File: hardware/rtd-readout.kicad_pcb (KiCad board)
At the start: 4 copper layers, 122 x 82 mm, 34 parts, among them J1 Conn_RTD_4W, J2 Conn_RTD_4W, J3 Conn_RTD_4W, J4 Conn_T7_Analog, J5 Conn_T7_I2C, J6 Conn_Power, U1 ADS1115IDGS (0x48), U2 ADS1115IDGS (0x49)

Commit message: rev-C: 4th channel — CH4 on U2's spare AIN2/3, J4 2x5, board grown south
board_spec 3->4ch. Schematic: page 4 (D4/R6/J7/TP11/TP12), U2 AIN2/3 wired,
Conn_T7_Analog 2x5 (CH4 sense on pins 9/10, AGND kept on 7/8); netlist delta
verified exactly the CH4 additions (21->23 nets). Library: 2x05 footprint +
symbol updated (embedded/library kept identical). Layout via pcbnew: board
122x82->122x104, holes moved, planes extended+refilled, CH4 placed/routed,
CH2_SENSE- rerouted off the new J4 row, one VS via relocated. ERC 0/0 (all
severities), DRC 0/0, parity 60 (metadata only), SPICE 7/7. Verified by
5-agent workflow (delta oracle, gates, adversarial layout review incl.
single-point GND tie intact, visual audit 4 pages + board, BOM=35); its
findings (library symbol mismatch, 2 label collisions) fixed and re-gated.

Co-Authored-By: Claude Opus 4.8 <noreply@anthropic.com>
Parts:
- added D4: CRD ~220uA, D_MELF, F.Cu at (44.0, 84.0)
- added J7: Conn_RTD_4W, TerminalBlock_Phoenix_MKDS-1,5-4-5.08_1x04_P5.08mm_Horizontal, F.Cu at (9.00, 78.0)
- added R6: 910R, R_1206_3216Metric, F.Cu at (53.0, 84.0)
- added TP11: TestPoint, TestPoint_Pad_D1.5mm, F.Cu at (51.5, 80.0)
- added TP12: TestPoint, TestPoint_Pad_D1.5mm, F.Cu at (58.0, 86.0)
- J4: footprint rtd-readout:PinHeader_2x04_P2.54mm_Vertical -> PinHeader_2x05_P2.54mm_Vertical
- moved ? 22.0 mm to (4.00, 100.0)
- moved ? 22.0 mm to (118.0, 100.0)
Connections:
- U2 pad 6: unconnected-(U2-AIN2-Pad6) -> CH4_TOP
- U2 pad 7: unconnected-(U2-AIN3-Pad7) -> CH4_MID
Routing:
- net CH4_MID: track 0.00 -> 98.8 mm
- net CH4_SENSE-: track 0.00 -> 61.5 mm
- net CH4_SENSE+: track 0.00 -> 53.9 mm
- net CH4_TOP: track 0.00 -> 50.6 mm
- net CH2_SENSE-: track 34.1 -> 38.8 mm
- net +5V: track 10.7 -> 13.2 mm, vias 5 -> 6
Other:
- board size 122 x 82 mm -> 122 x 104 mm

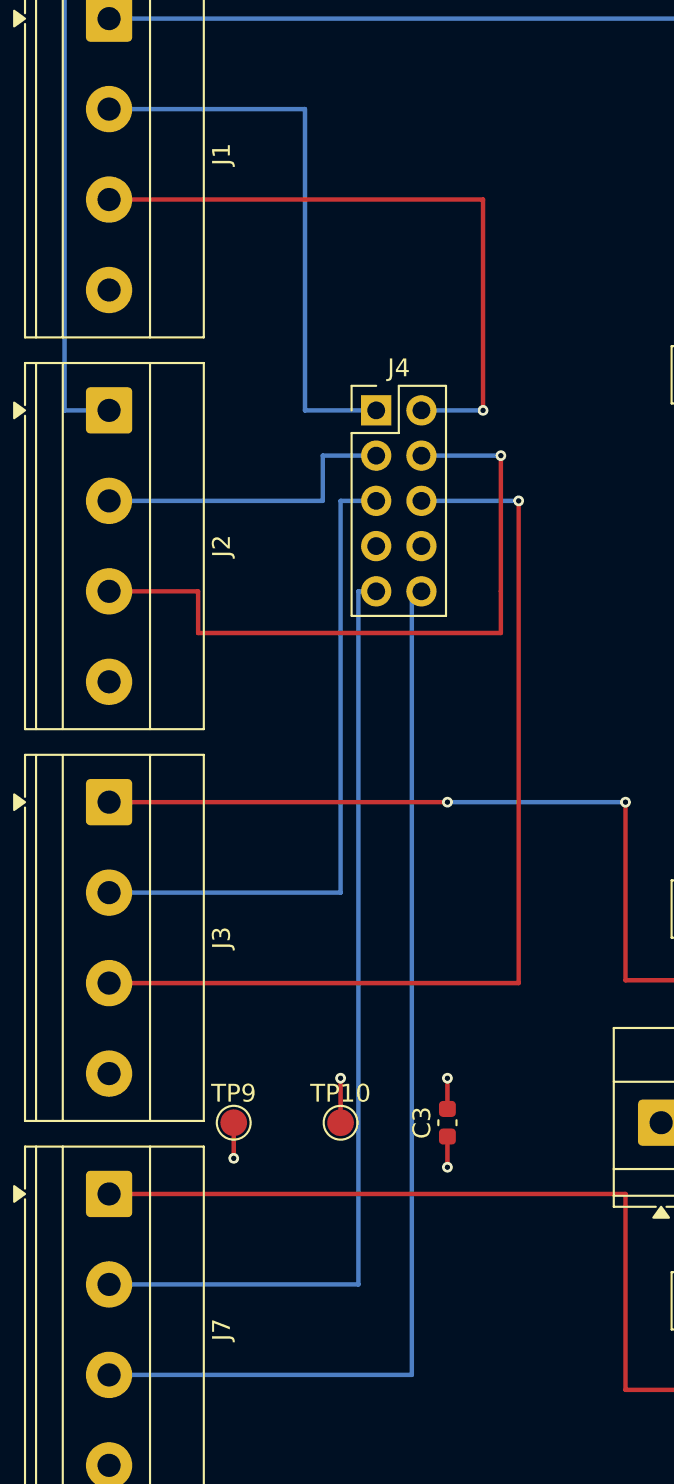
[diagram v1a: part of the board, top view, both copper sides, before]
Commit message: rev-D: sense-line RC filters fitted (1k per leg + 0.1uF diff at J4, x4 ch)
Schematic: R7-R14 inline in CHn_SENSE+/- + C5-C8 differential; filtered nets
CHn_T7+/- labeled; netlist delta = exactly the filter insertion (23->31 nets,
oracle mutation-tested). Layout: Rs inline in existing legs (F-inline or
via-sandwich), caps on B.Cu across J4 pin pairs (courtyard-less variant);
ERC 0/0, DRC 0/0/0 (parity 84 metadata-only, 0 net conflicts); adversarial
copper review: all 8 filters genuinely in series, min clearance 0.315mm,
GND tie untouched. SPICE 7/7 - test5 now models fitted hardware. Fleet
visual findings fixed (text de-stacking, label moves, silk offsets, zero-
length residue). Closes the Session-006 open decision (USER_MANUAL 8.5).

Co-Authored-By: Claude Opus 4.8 <noreply@anthropic.com>
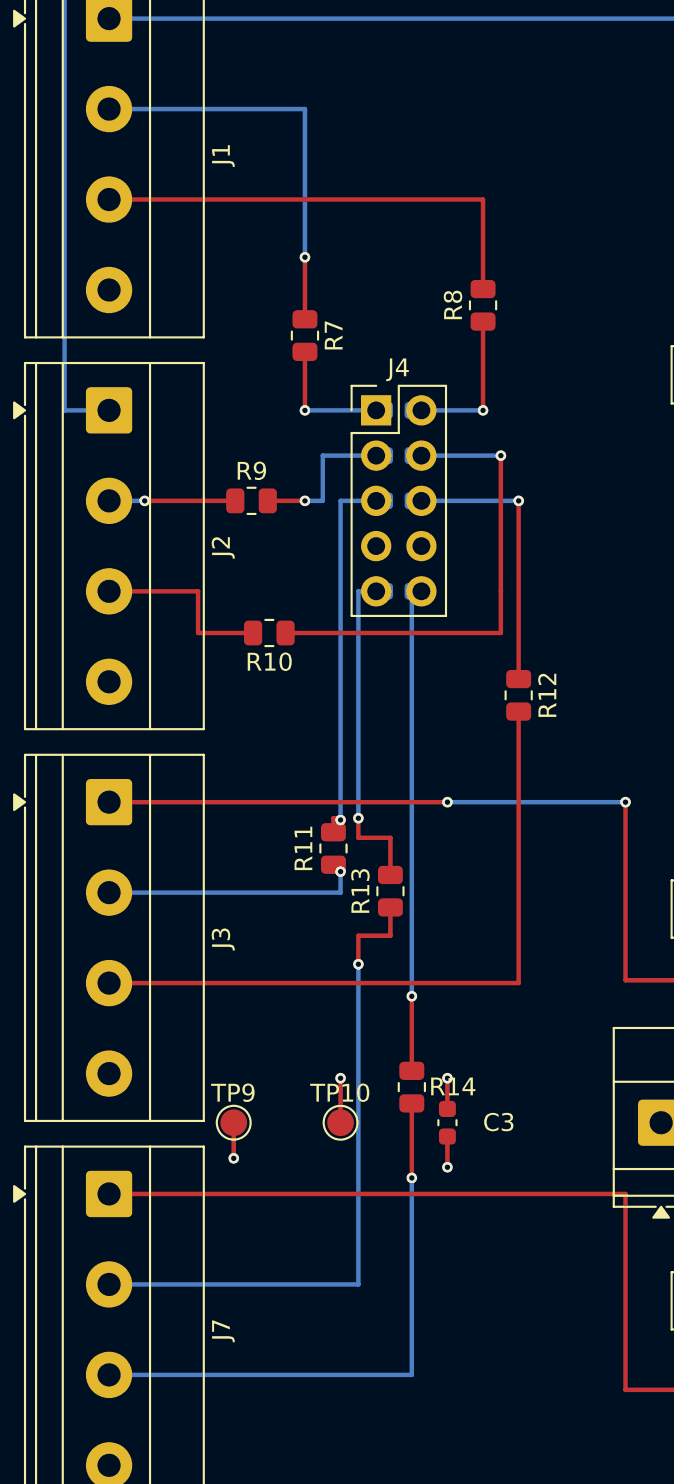
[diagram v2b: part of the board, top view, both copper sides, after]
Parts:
- added C5: 0.1uF, C_0603_1608Metric, B.Cu at (25.3, 34.0)
- added C6: 0.1uF, C_0603_1608Metric, B.Cu at (25.3, 36.5)
- added C7: 0.1uF, C_0603_1608Metric, B.Cu at (25.3, 39.1)
- added C8: 0.1uF, C_0603_1608Metric, B.Cu at (25.3, 44.2)
- added R10: 1k, R_0805_2012Metric, F.Cu at (18.0, 46.5)
- added R11: 1k, R_0805_2012Metric, F.Cu at (21.6, 58.6)
- added R12: 1k, R_0805_2012Metric, F.Cu at (32.0, 50.0)
- added R13: 1k, R_0805_2012Metric, F.Cu at (24.8, 61.0)
- added R14: 1k, R_0805_2012Metric, F.Cu at (26.0, 72.0)
- added R7: 1k, R_0805_2012Metric, F.Cu at (20.0, 29.8)
- added R8: 1k, R_0805_2012Metric, F.Cu at (30.0, 28.1)
- added R9: 1k, R_0805_2012Metric, F.Cu at (17.0, 39.1)
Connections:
- J4 pad 1: CH1_SENSE+ -> CH1_T7+
- J4 pad 10: CH4_SENSE- -> CH4_T7-
- J4 pad 2: CH1_SENSE- -> CH1_T7-
- J4 pad 3: CH2_SENSE+ -> CH2_T7+
- J4 pad 4: CH2_SENSE- -> CH2_T7-
- J4 pad 5: CH3_SENSE+ -> CH3_T7+
- J4 pad 6: CH3_SENSE- -> CH3_T7-
- J4 pad 9: CH4_SENSE+ -> CH4_T7+
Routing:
- net CH4_SENSE-: track 61.5 -> 32.2 mm, vias 0 -> 1
- net CH2_SENSE-: track 38.8 -> 10.4 mm, vias 1 -> 0
- net CH4_T7-: track 0.00 -> 27.4 mm, vias 0 -> 1
- net CH2_T7-: track 0.00 -> 26.5 mm, vias 0 -> 1
- net CH3_SENSE+: track 37.0 -> 14.9 mm, vias 0 -> 1
- net CH3_T7+: track 0.00 -> 21.2 mm, vias 0 -> 1
- net CH4_T7+: track 0.00 -> 18.7 mm, vias 0 -> 1
- net CH3_SENSE-: track 55.5 -> 38.2 mm, vias 1 -> 0
- net CH4_SENSE+: track 53.9 -> 37.0 mm, vias 0 -> 1
- net CH3_T7-: track 0.00 -> 15.4 mm, vias 0 -> 1
- net CH2_SENSE+: track 17.5 -> 6.59 mm, vias 0 -> 1
- net CH1_SENSE-: track 36.3 -> 26.0 mm, vias 1 -> 0
- net CH1_SENSE+: track 31.9 -> 22.8 mm, vias 0 -> 1
- net CH1_T7-: track 0.00 -> 8.41 mm, vias 0 -> 1
- net CH2_T7+: track 0.00 -> 8.13 mm, vias 0 -> 1
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
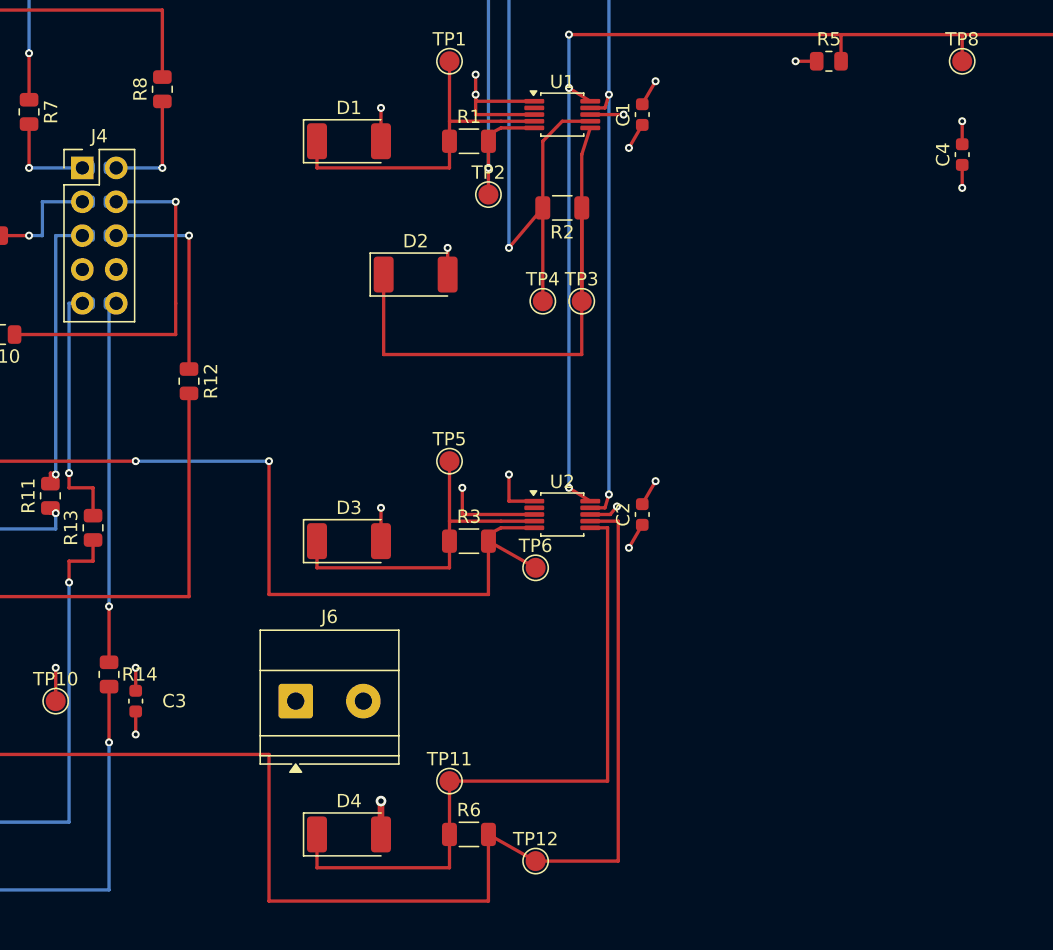
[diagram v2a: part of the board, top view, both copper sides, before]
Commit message: rev-E: DFM/availability respin - CRD J500 TO-92, 0805 caps, R_ref 820R
Hand-assembly + live-Digi-Key-verified changes (all adversarially fact-checked):
- D1-D4: CDLL5283 MELF (unbuyable, 0 stock/40wk MOQ) -> LIS J500 TO-92 2L;
  new mirrored footprint TO-92-2_CRD-J500 (pad1=K at flat-to-silk insertion,
  0.8mm drill), 8 F.Cu stubs bridge old MELF trace ends to the THT pads.
- C1-C8: 0603 -> 0805 (Samsung CL21B104KBCNNNC / CL21A106KACLRNC; old Murata
  parts obsolete/backordered). C5-C8 keep the back-side across-J4 scheme.
- R_ref: 910R -> 820R (KOA RN73H2BTTD8200B10, 0.1%, 10ppm/C) - J500 band is
  +/-20%, 910R would clip the ADS1115 +/-0.256V range at band max.
- SPICE harness re-pointed (240uA, 820R, VL 1.2V, Z 4Meg; test4 gate <95% FS
  at kc=1.2); docs/spec/BOM_REVIEW/host defaults updated.

Gates: ERC 0/0, DRC 0 violations / 0 unconnected, SPICE 7/7 PASS
(t4: V_ref at band max = 237 mV = 93% FS, 14.9 bits).

Co-Authored-By: Claude Fable 5 <noreply@anthropic.com>
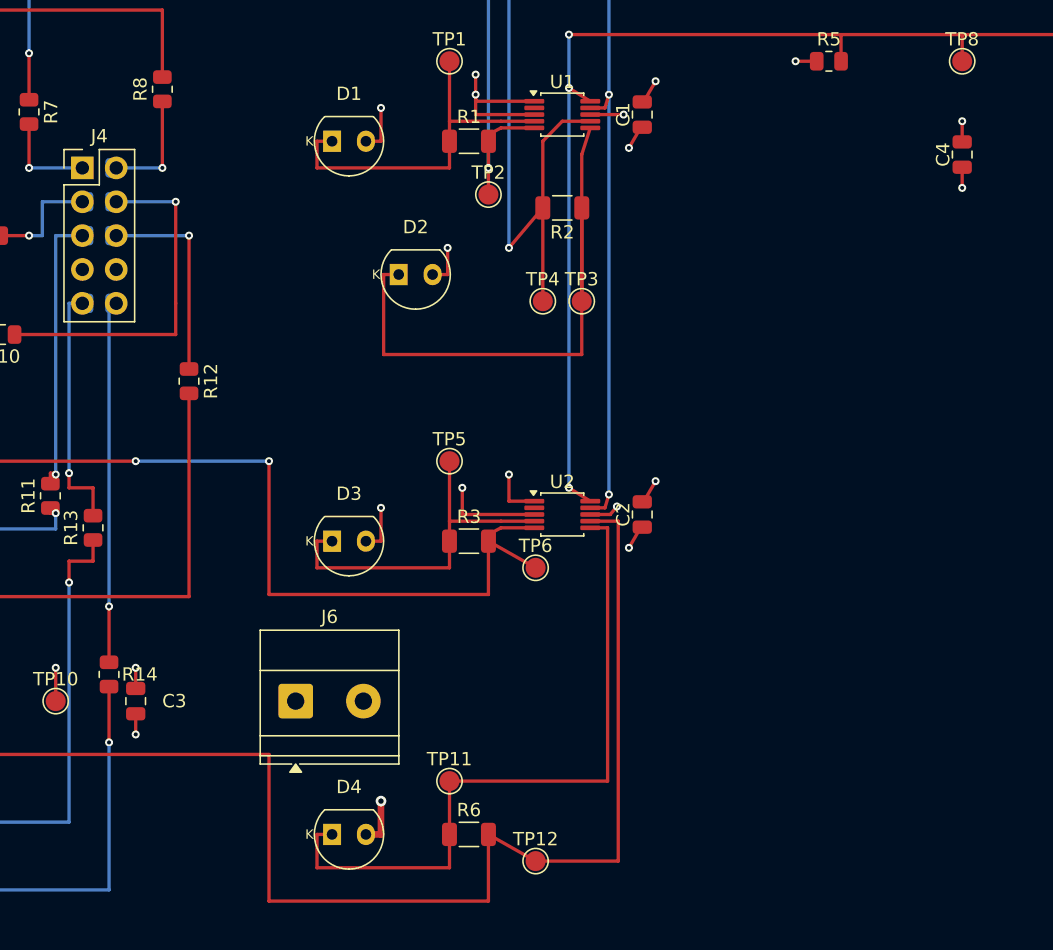
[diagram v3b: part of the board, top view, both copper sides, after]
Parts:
- C1, C2, C3, C4: footprint rtd-readout:C_0603_1608Metric -> rtd-readout:C_0805_2012Metric
- C5, C6, C7, C8: footprint C_0603_1608Metric -> rtd-readout:C_0805_2012Metric
- D1, D2, D3: value CRD ~220uA -> CRD ~240uA; footprint rtd-readout:D_MELF -> rtd-readout:TO-92-2_CRD-J500
- D4: value CRD ~220uA -> CRD ~240uA; footprint D_MELF -> rtd-readout:TO-92-2_CRD-J500
- R1, R2, R3, R6: value 910R -> 820R
- moved D1 1.27 mm to (42.7, 32.0)
- moved D2 1.27 mm to (47.7, 42.0)
- moved D3 1.27 mm to (42.7, 62.0)
- moved D4 1.27 mm to (42.7, 84.0)
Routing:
- net +5V: track 13.2 -> 17.7 mm
- net CH4_TOP: track 50.6 -> 51.7 mm
- net CH3_TOP: track 26.3 -> 27.4 mm
- net CH2_TOP: track 45.0 -> 46.1 mm
- net CH1_TOP: track 26.3 -> 27.4 mm

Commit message: rev-F: cryostat/stability respin - 100uA S-101T CRD, C0G sense path, 2ppm R_ref
Sensors are in a vacuum cryostat down to ~100 K; excitation lowered to cut
self-heating ~6x (0.3-1.6 uW nominal), measurement path upgraded to
precision-grade passives. All parts live-verified on Digi-Key with
adversarial fact-checks:
- D1-D4: LIS J500 TO-92 -> SEMITEC S-101T (100uA typ, band 0.05-0.21mA,
  SMD flat 2-lead); custom footprint from SEMITEC's recommended land
  pattern (1.2x1.6mm pads, 3.4mm centers, cathode-band marking).
- R_ref: 820R 10ppm -> 1.00k +/-0.05% +/-2ppm/C (Vishay TNPU12061K00AWEN00);
  V_ref 100mV nom, 210mV = 82% FS at band max. Reference is no longer the
  drift limiter (by design).
- C5-C8: X7R 0805 -> C0G/NP0 0.1uF 50V 1206 (Murata GRM31C5C1H104JA01L);
  moved east of J4 on B.Cu with routed stubs (1206 body cannot straddle
  the pin holes). R7-R14: 1% thick film -> 0.1% 25ppm thin film (Susumu).
- Sims: 100uA/1k/2ppm/VL 2.0/RTD window extended to 100 K (Pt100 29.5R);
  band sweeps 0.5-2.1x; t3 criterion re-gated to 'R_ref not limiting';
  t6 noise assumption made per-read (4-conversion average).

Gates: ERC 0/0, DRC 0 violations / 0 unconnected, SPICE 7/7 PASS.

Co-Authored-By: Claude Fable 5 <noreply@anthropic.com>
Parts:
- C5, C6, C7, C8: footprint rtd-readout:C_0805_2012Metric -> rtd-readout:C_1206_3216Metric
- D1, D2, D3, D4: value CRD ~240uA -> CRD ~100uA; footprint rtd-readout:TO-92-2_CRD-J500 -> rtd-readout:D_SEMITEC_S-101T
- R1, R2, R3, R6: value 820R -> 1k
- moved C5 9.23 mm to (34.5, 34.0)
- moved C6 9.23 mm to (34.5, 36.5)
- moved C7 9.23 mm to (34.5, 39.1)
- moved C8 9.23 mm to (34.5, 44.2)
- moved D1 1.27 mm to (44.0, 32.0)
- moved D2 1.27 mm to (49.0, 42.0)
- moved D3 1.27 mm to (44.0, 62.0)
- moved D4 1.27 mm to (44.0, 84.0)
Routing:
- net CH3_T7+: track 21.2 -> 37.0 mm
- net CH2_T7+: track 8.13 -> 24.0 mm
- net CH1_T7+: track 7.25 -> 23.1 mm
- net CH4_T7+: track 18.7 -> 34.6 mm
- net CH4_T7-: track 27.4 -> 33.9 mm
- net CH3_T7-: track 15.4 -> 21.9 mm
- net CH1_T7-: track 8.41 -> 14.9 mm
- net CH2_T7-: track 26.5 -> 33.0 mm
- net +5V: track 17.7 -> 16.0 mm
